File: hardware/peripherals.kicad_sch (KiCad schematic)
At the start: 23 parts, among them J1 Conn_01x02, J2 Conn_01x03, J3 USB_C_Receptacle_USB2.0_14P, SW1 SW_Push, U1 74AHCT1G125, U2 DS3231MZ, U3 USBLC6-2SC6

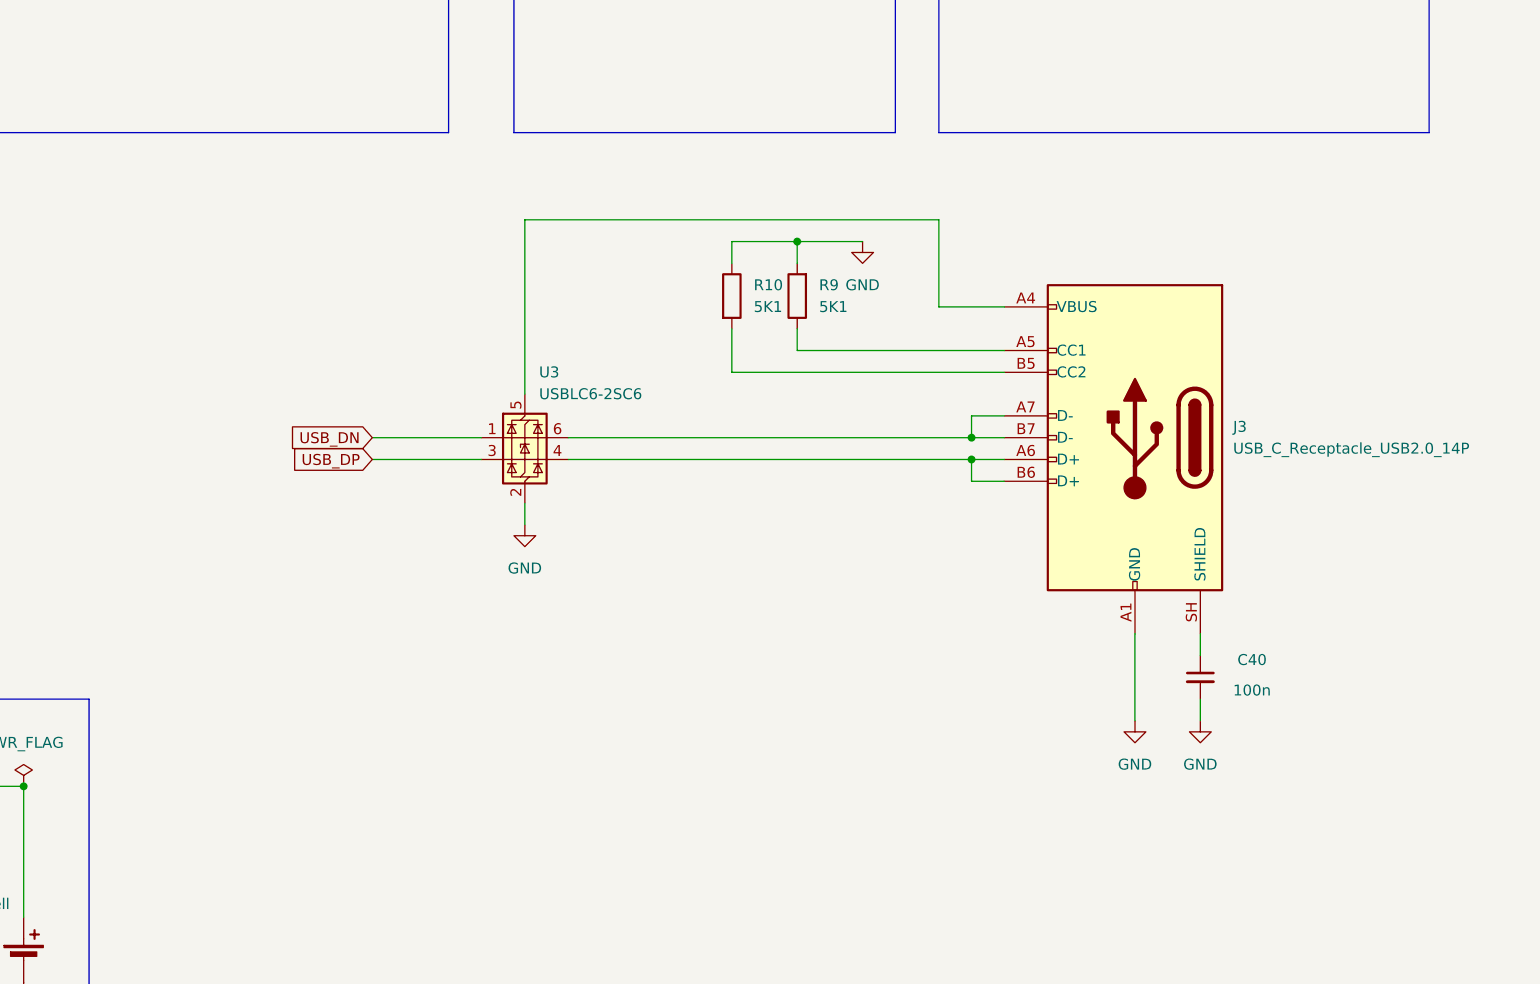
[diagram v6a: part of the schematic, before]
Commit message: Ethernet: add RB1-125B8G1A Gigabit MagJack with LEDs
- RJ45 with integrated magnetics (10/100/1000 BaseT)
- 4 differential pairs connected to CM4 Ethernet PHY
- Center tap biased via 10Ω + 100nF to 3.3V
- Green/Yellow LEDs wired to ETH_nLED1/nLED2
- ETH_SYNC_IN/OUT and ETH_nLED3 NC'd
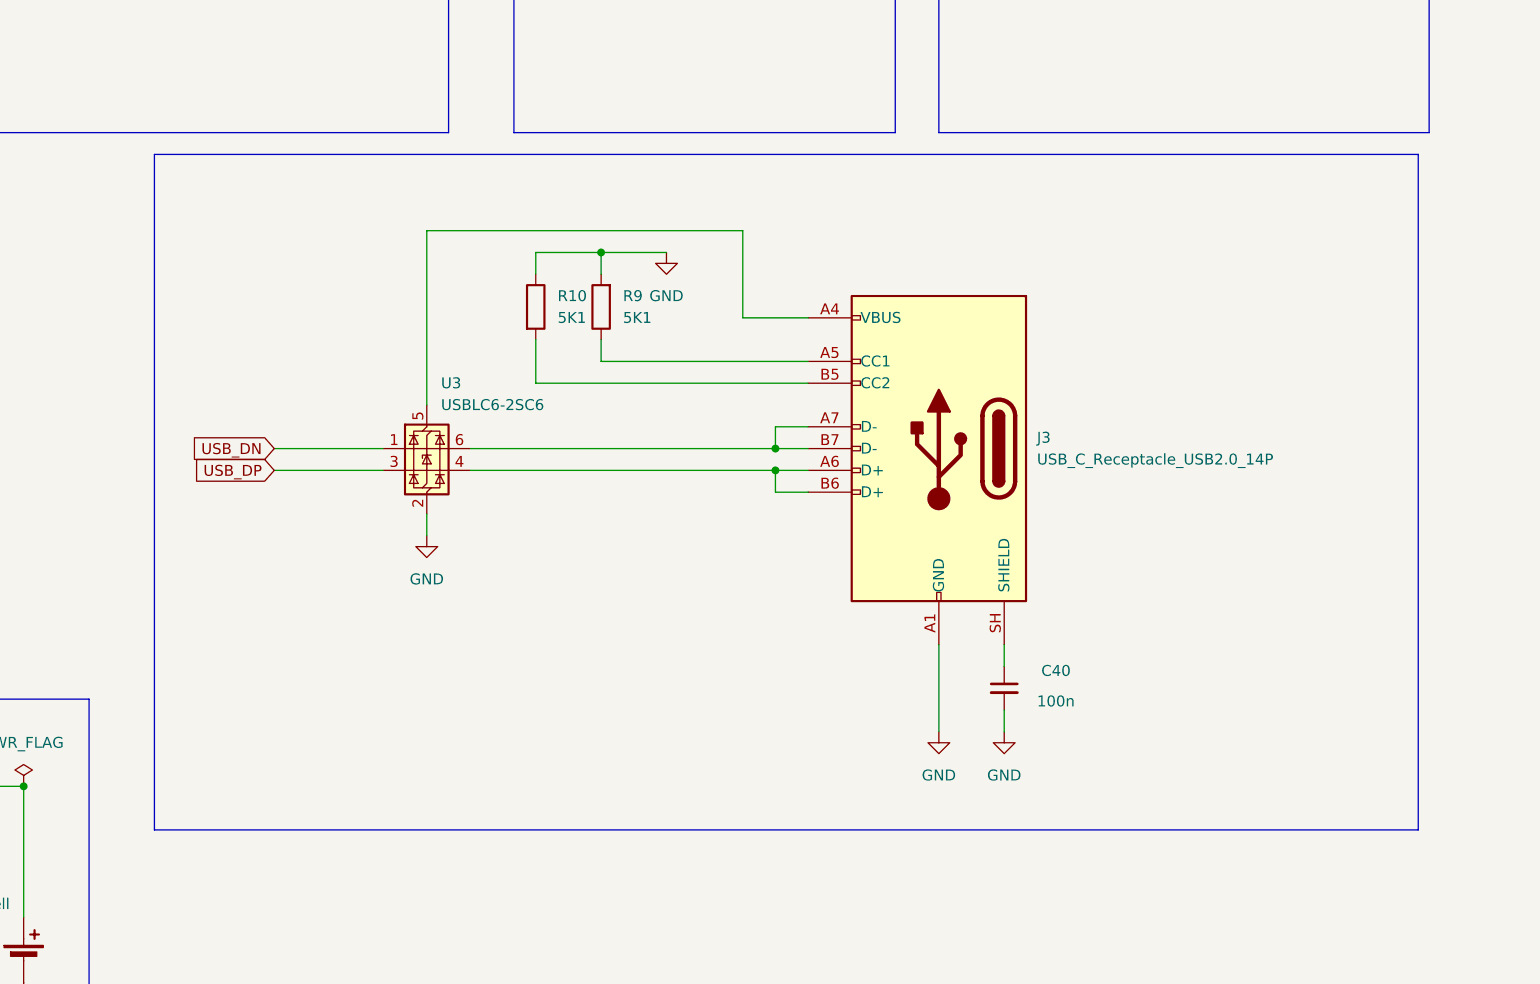
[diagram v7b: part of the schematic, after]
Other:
- moved on the sheet: C40, J3, R10, R9, U3

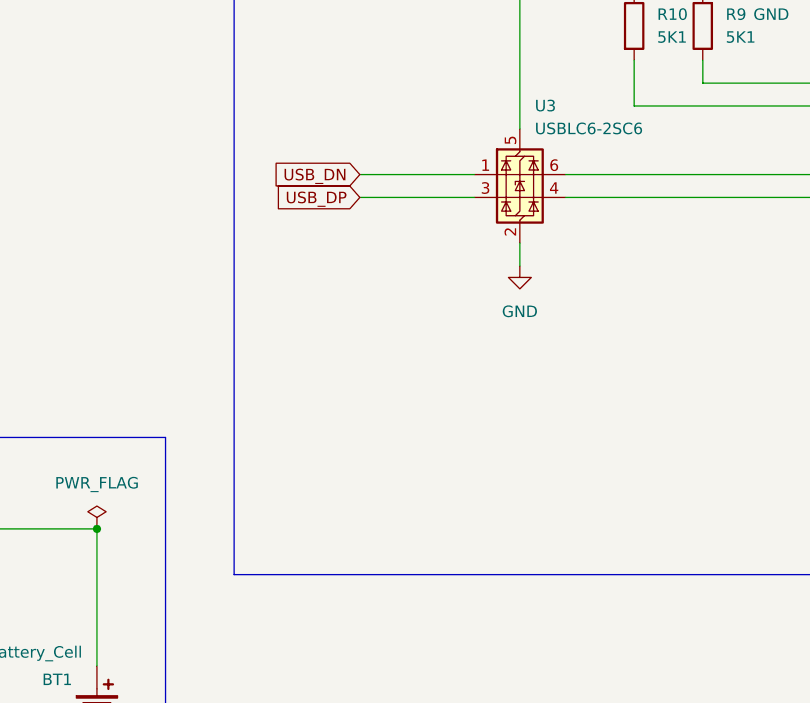
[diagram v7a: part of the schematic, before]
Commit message: Clean up ERC: PWR_FLAGs, OTG_ID solder jumper, PCIe_CLK_nREQ
- Add PWR_FLAG on GND net (PSU sheet)
- USB_OTG_ID: solder jumper to GND with 10K pull-up for host/device mode
- PCIe_CLK_nREQ tied to GND locally on connector 2
- 1 ERC error remaining: CM4 dual 3.3V output pins (false positive)
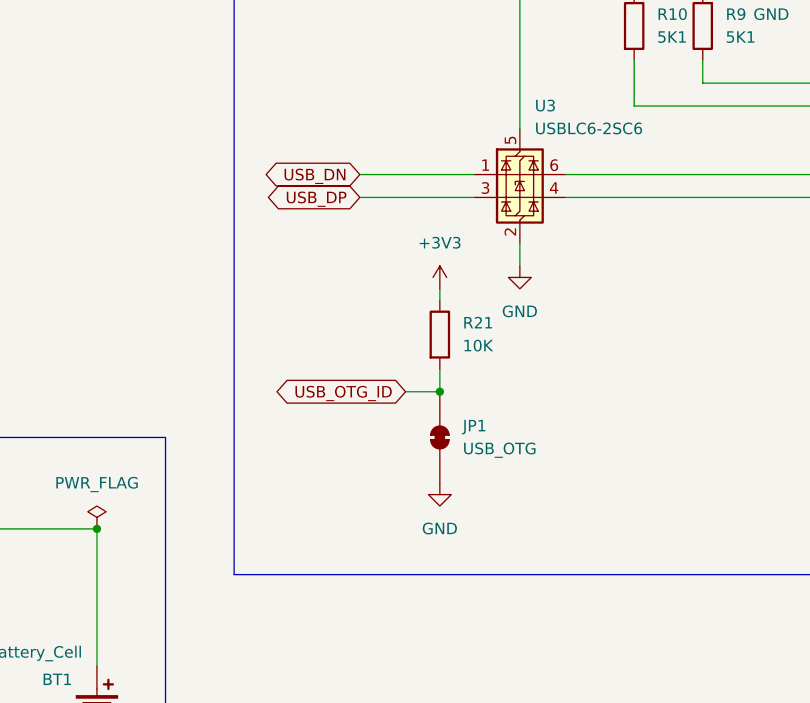
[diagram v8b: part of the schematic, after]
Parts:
- added JP1: USB_OTG, symbol Jumper:SolderJumper_2_Bridged
- added R21: 10K, symbol Device:R
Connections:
- net +3V3: now also R21.1
- net GND: now also JP1.1 (A)
- new net USB_OTG_ID: JP1.2 (B), R21.2
